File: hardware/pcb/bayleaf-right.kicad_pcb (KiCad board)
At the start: 2 copper layers, 135.5 x 89.5 mm, 64 parts, among them SW1 PG1316S, SW10 PG1316S, SW11 PG1316S, SW12 PG1316S, SW13 PG1316S, SW14 PG1316S, SW15 PG1316S, SW16 PG1316S, SW17 PG1316S, SW18 PG1316S, SW19 PG1316S, SW2 PG1316S, SW20 PG1316S, SW21 PG1316S, SW22 PG1316S, SW23 PG1316S, SW24 PG1316S, SW25 PG1316S, SW26 PG1316S, SW27 PG1316S, SW28 PG1316S, SW29 PG1316S, SW3 PG1316S, SW30 PG1316S, SW31 TS-1187A-B-A-B, SW32 MSK12C02, SW4 PG1316S, SW5 PG1316S, SW6 PG1316S, SW7 PG1316S, SW8 PG1316S, SW9 PG1316S, U1 nice!nano v2

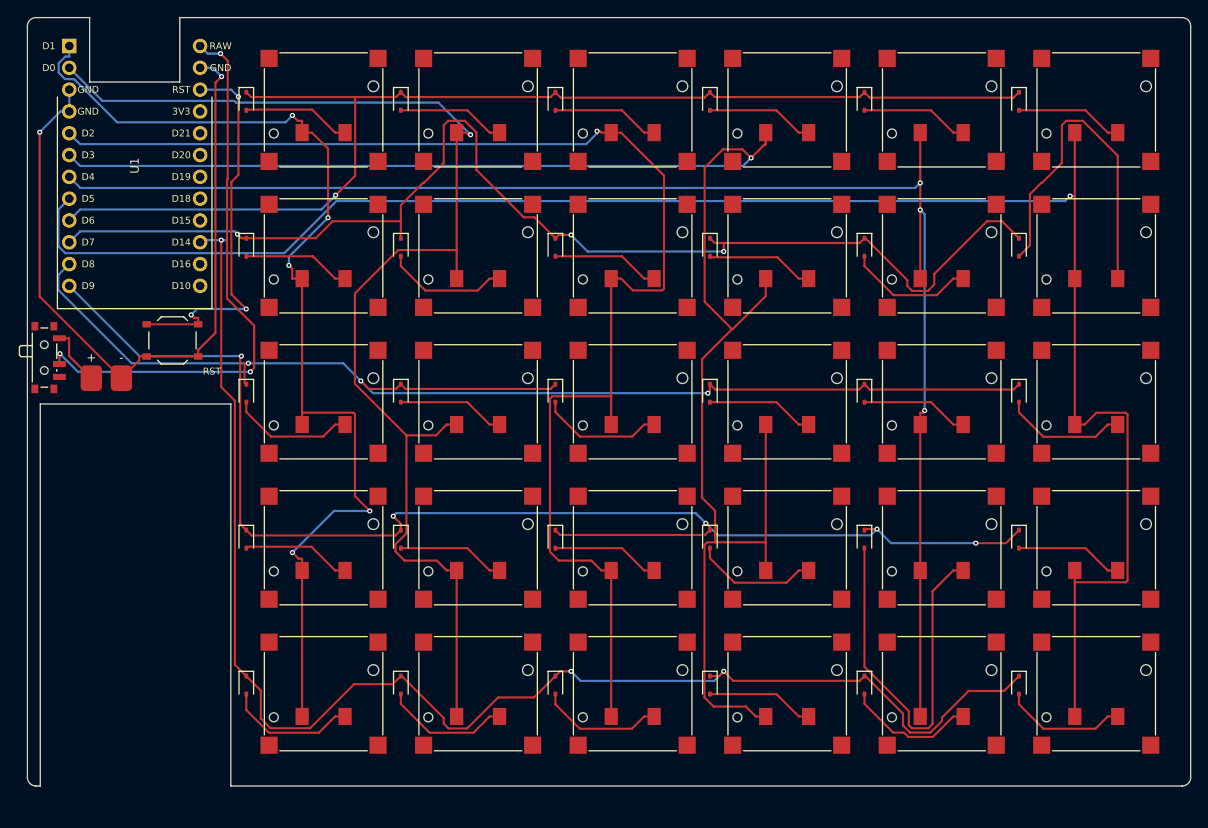
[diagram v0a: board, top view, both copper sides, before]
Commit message: Case: rebuild after the original's MK5 drawing (shell + lid over controller)
- hardware/case: top shell with 103 x 86 key window, 2 mm divider, 27 mm
  controller bay closed by a 0.8 mm roof, 6.2 -> 3.8 mm front curve, drafted
  walls, 7 tapped M2 bosses; separate 0.8 mm bottom plate screwed into them
- PCB: 17 mm pitch to fit the window, SOD-523 diodes, nice!nano rotated so
  USB-C exits the front, 402040 cell under the roof, 2.2 mm holes + copper
  keep-outs at the bosses, per-half matrix pin map; both halves route clean
- firmware: per-half kscan pins in the left/right overlays
- docs: case-drawing notes, BOM/ordering/assembly/schematic, new renders

Co-Authored-By: Claude Opus 5.5 <noreply@anthropic.com>
Claude-Session: https://claude.ai/code/session_01C1HRLCKaYQawWFomwAvAgT
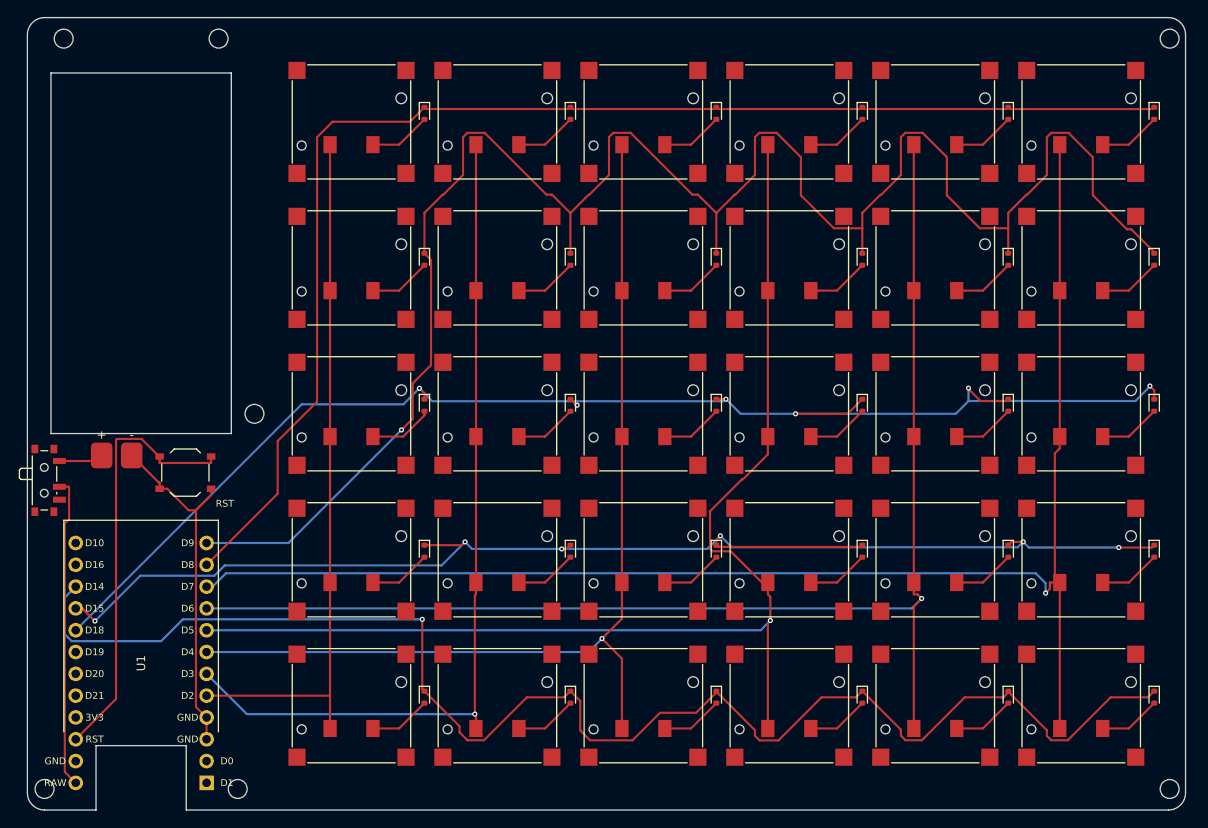
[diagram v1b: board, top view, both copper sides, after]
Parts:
- added H1: boss 6, MountingHole:MountingHole_2.2mm_M2, F.Cu at (133.1, 2.45)
- added H2: boss 6, MountingHole:MountingHole_2.2mm_M2, F.Cu at (133.1, 89.8)
- added H3: boss 6, MountingHole:MountingHole_2.2mm_M2, F.Cu at (22.3, 2.45)
- added H4: boss 6, MountingHole:MountingHole_2.2mm_M2, F.Cu at (4.23, 2.45)
- added H5: boss 6, MountingHole:MountingHole_2.2mm_M2, F.Cu at (26.4, 46.1)
- added H6: boss 4, MountingHole:MountingHole_2.2mm_M2, F.Cu at (24.5, 89.8)
- added H7: boss 4, MountingHole:MountingHole_2.2mm_M2, F.Cu at (2.00, 89.8)
- D1, D10, D11, D12, D13, D14, D15, D16, D17, D18, D19, D2, D20, D21, D22, D23, D24, D25, D26, D27, D28, D29, D3, D30, D4, D5, D6, D7, D8, D9: value 1N4148WS -> 1N4148WT; footprint Diode_SMD:D_SOD-323 -> Diode_SMD:D_SOD-523
- moved U1 58.0 mm to (13.2, 75.2), turned to 180 degrees
- moved D12 20.8 mm to (46.2, 28.1)
- moved D18 20.8 mm to (46.2, 45.1)
- moved D24 20.8 mm to (46.2, 62.1)
- moved D30 20.8 mm to (46.2, 79.2)
- moved D6 20.8 mm to (46.2, 11.2)
- moved D11 19.8 mm to (63.2, 28.1)
- moved D17 19.8 mm to (63.2, 45.1)
- moved D23 19.8 mm to (63.2, 62.1)
- moved D29 19.8 mm to (63.2, 79.2)
- moved D5 19.8 mm to (63.2, 11.2)
- moved D10 18.8 mm to (80.2, 28.1)
- moved D16 18.8 mm to (80.2, 45.1)
- moved D22 18.8 mm to (80.2, 62.1)
- moved D28 18.8 mm to (80.2, 79.2)
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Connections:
- U1 pad 1: COL0 -> (no net)
- U1 pad 10: ROW1 -> COL5
- U1 pad 11: ROW2 -> ROW0
- U1 pad 12: ROW3 -> ROW1
- U1 pad 14: GND -> (no net)
- U1 pad 2: COL1 -> (no net)
- U1 pad 20: (no net) -> ROW2
- U1 pad 21: (no net) -> ROW3
- U1 pad 5: COL2 -> COL0
- U1 pad 6: COL3 -> COL1
- U1 pad 7: COL4 -> COL2
- U1 pad 8: COL5 -> COL3
- U1 pad 9: ROW0 -> COL4
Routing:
- net ROW1: track 142.9 -> 221.8 mm, vias 3 -> 1
- net COL3: track 195.4 -> 142.0 mm
- net COL1: track 147.1 -> 101.3 mm
- net GND: track 86.5 -> 41.0 mm, vias 2 -> 0
- net COL2: track 159.8 -> 116.6 mm
- net COL0: track 124.7 -> 82.4 mm, vias 5 -> 0
- net COL5: track 210.9 -> 170.8 mm
- net N_SW20: track 45.9 -> 7.22 mm
- net N_SW7: track 40.1 -> 7.22 mm
- net RAW: track 66.0 -> 36.4 mm, vias 3 -> 0
- net COL4: track 176.6 -> 152.8 mm, vias 3 -> 1
- net ROW0: track 137.0 -> 154.9 mm, vias 1 -> 0
- net ROW2: track 149.5 -> 160.9 mm, vias 3 -> 6
- net N_SW30: track 15.2 -> 7.22 mm
- net N_SW26: track 15.2 -> 7.22 mm
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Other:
- board size 135.5 x 89.5 mm -> 134.9 x 92.3 mm
- board text added: "LiPo 4.0x20x40"
- board text removed: "LiPo 3.0x20x40"

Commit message: Case: match the build photos - 5 mm tall, separate controller lid
- shell: 3.8 mm frame around the key window curving up to 4.1 mm at the
  controller end; controller bay now open on top; all posts M2 x 2
- new lid part: 0.8 mm plate over the bay, flush with the outer edges, taped
  on; its top is the 5.0 mm tallest point (contrast anodised like the original)
- 302040 cell (bay under the lid is 3.4 mm), 14 x M2x3 screws
- renders: silver shell, blue lid, blank caps; desk/front views like the photos
- docs/BOM/README updated; PCB unchanged

Co-Authored-By: Claude Opus 5.5 <noreply@anthropic.com>
Claude-Session: https://claude.ai/code/session_01C1HRLCKaYQawWFomwAvAgT
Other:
- board text added: "LiPo 3.0x20x40"
- board text removed: "LiPo 4.0x20x40"
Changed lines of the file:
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@@
     (effects (font (size 0.8 0.8) (thickness 0.12)))
   )
-  (gr_text "LiPo 4.0x20x40" (at 13.25 27) (layer "Cmts.User")
+  (gr_text "LiPo 3.0x20x40" (at 13.25 27) (layer "Cmts.User")
     (effects (font (size 0.9 0.9) (thickness 0.135)))
   )

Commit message: Case: one-piece shell from the sketchpad shape (3.2 mm rim, 5.0 mm plateau, S-bends)
- case.py: top surface = blurred square plateau (x >= 96.5, y <= 76) over a 3.2 mm rim;
  controller roofed by the shell (no lid), R2 key-window corners, USB-C in the back wall,
  reset pin-hole, per-post thread depths (2 mm / 1.1 mm)
- PCB: nice!nano USB-C facing the back, KMR2 reset and slide switch beside it, 302030 cell
  window in front of it; rerouted, fab outputs regenerated
- firmware: per-half matrix pins to match the new layout
- docs: sketchpad shape saved, renders, BOM/ordering/assembly/case/schematic updated

Co-Authored-By: Claude Opus 5.5 <noreply@anthropic.com>
Claude-Session: https://claude.ai/code/session_01C1HRLCKaYQawWFomwAvAgT
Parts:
- BT1: footprint bayleaf:Battery_Pads -> bayleaf:Battery_Pads_Small
- H3, H4: value boss 6 -> boss 4
- H6, H7: value boss 4 -> boss 6
- SW31: value TS-1187A-B-A-B -> KMR211NGLFS; footprint Button_Switch_SMD:SW_Push_1P1T_XKB_TS-1187A -> Button_Switch_SMD:SW_Push_1P1T_NO_CK_KMR2
- moved U1 58.2 mm to (13.6, 17.0), turned to 0 degrees
- moved SW32 38.9 mm to (2.10, 15.0)
- moved SW31 31.6 mm to (24.8, 22.0), turned to -90 degrees
- moved BT1 24.2 mm to (2.15, 28.2)
- moved H3 2.48 mm to (24.8, 2.45)
- moved H4 2.23 mm to (2.00, 2.45)
- moved H6 2.23 mm to (22.3, 89.8)
- moved H7 2.23 mm to (4.23, 89.8)
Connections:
- U1 pad 10: COL5 -> ROW2
- U1 pad 11: ROW0 -> ROW1
- U1 pad 12: ROW1 -> ROW0
- U1 pad 17: (no net) -> COL0
- U1 pad 18: (no net) -> COL1
- U1 pad 19: (no net) -> COL2
- U1 pad 20: ROW2 -> COL3
- U1 pad 21: ROW3 -> COL4
- U1 pad 22: ROW4 -> COL5
- U1 pad 5: COL0 -> (no net)
- U1 pad 6: COL1 -> (no net)
- U1 pad 7: COL2 -> (no net)
- U1 pad 8: COL3 -> ROW4
- U1 pad 9: COL4 -> ROW3
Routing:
- net ROW3: track 158.7 -> 199.0 mm
- net ROW4: track 169.9 -> 207.6 mm
- net ROW1: track 221.8 -> 187.9 mm, vias 1 -> 4
- net RST: track 50.5 -> 17.7 mm
- net COL2: track 116.6 -> 129.5 mm, vias 1 -> 3
- net BAT+: track 5.19 -> 15.6 mm
- net ROW0: track 154.9 -> 146.1 mm, vias 0 -> 1
- net COL3: track 142.0 -> 134.3 mm
- net RAW: track 36.4 -> 30.0 mm
- net GND: track 41.0 -> 47.4 mm
- net COL5: track 170.8 -> 176.0 mm
- net COL0: track 82.4 -> 84.6 mm, vias 0 -> 1
- net COL4: track 152.8 -> 150.6 mm
- net ROW2: track 160.9 -> 161.5 mm, vias 6 -> 5
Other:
- outline, holes or cut-outs redrawn
- board text added: "LiPo 3.0x20x30"
- board text removed: "LiPo 3.0x20x40"

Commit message: Drop the power switch, stadium USB-C opening, straight-wall + chamfer case variant
- PCB: no slide switch; the cell feeds the nice!nano RAW pin directly (ZMK deep sleep);
  rerouted, 0 unconnected, courtyard warning gone
- case: obround USB-C opening concentric with the receptacle (continues into the plate
  edge), no switch slot; new bayleaf-shell-*-chamfer variant with vertical walls and a
  1 mm 45 deg chamfer on the top edge that follows the blended surface
- renders: obround receptacle, compare.jpg (drafted vs chamfer); docs and BOM updated

Co-Authored-By: Claude Opus 5.5 <noreply@anthropic.com>
Claude-Session: https://claude.ai/code/session_01C1HRLCKaYQawWFomwAvAgT
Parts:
- removed SW32: MSK12C02, Button_Switch_SMD:SW_SPDT_PCM12
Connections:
- BT1 pad 1: BAT+ -> RAW
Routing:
- net ROW2: track 161.5 -> 178.6 mm, vias 5 -> 6
- net BAT+: track 15.6 -> 0.00 mm
- net ROW1: track 187.9 -> 202.6 mm, vias 4 -> 2
- net COL2: track 129.5 -> 116.7 mm, vias 3 -> 1
- net GND: track 47.4 -> 55.7 mm, vias 0 -> 1
- net COL1: track 100.8 -> 108.1 mm
- net COL5: track 176.0 -> 168.9 mm
- net ROW3: track 199.0 -> 192.9 mm
- net ROW0: track 146.1 -> 140.3 mm
- net ROW4: track 207.6 -> 204.2 mm
- net RAW: track 30.0 -> 32.7 mm
- net COL0: track 84.6 -> 86.6 mm
- net COL3: track 134.3 -> 135.0 mm

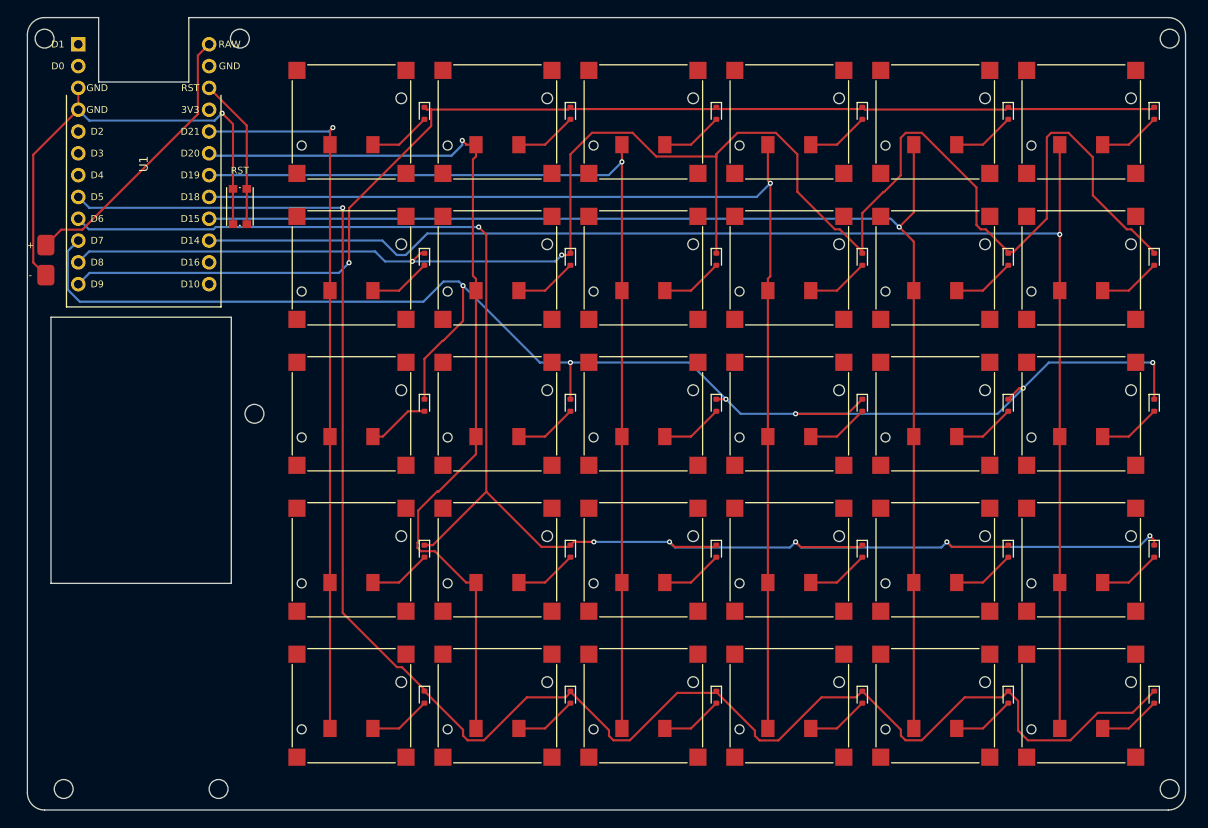
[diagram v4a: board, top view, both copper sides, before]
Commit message: Hand-solderable switches, FR4 bottom plate, reset button on the underside
- PCB: new Kailh_PG1316S_castellated footprint (window under each switch, contacts on plated
  half-holes, soldered from below with an iron; frame anchors on a small hotplate), after
  Mike Holscher's mikecinq, drawn from the Kailh land pattern. Order with castellated holes.
  Routing gets notched keepouts so Freerouting can reach the half-hole pads.
- Reset (KMR2) moves to the bottom side; the pin-hole in the plateau is gone.
- Bottom plate is now a copper-free 0.8 mm FR4 board (generate_pcb.py PlateBuilder, gerbers
  in fab/plate-*) so the radio isn't boxed in by aluminium; windows for the switch solder,
  nice!nano pins, reset button and USB-C.
- Renders (new underside view), BOM, ordering, assembly, case and schematic docs updated.

Co-Authored-By: Claude Opus 5.5 <noreply@anthropic.com>
Claude-Session: https://claude.ai/code/session_01C1HRLCKaYQawWFomwAvAgT
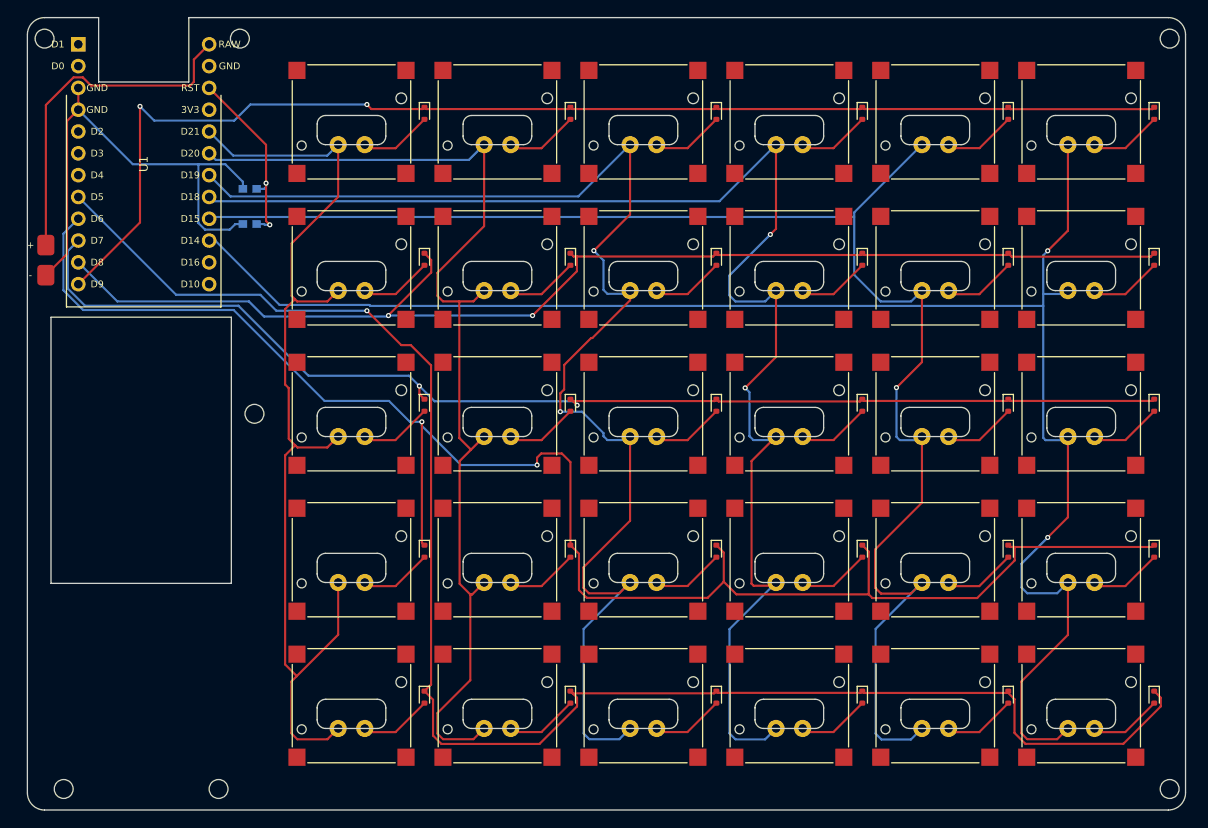
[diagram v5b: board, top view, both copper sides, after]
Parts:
- SW1, SW10, SW11, SW12, SW13, SW14, SW15, SW16, SW17, SW18, SW19, SW2, SW20, SW21, SW22, SW23, SW24, SW25, SW26, SW27, SW28, SW29, SW3, SW30, SW4, SW5, SW6, SW7, SW8, SW9: footprint bayleaf:Kailh_PG1316S -> bayleaf:Kailh_PG1316S_castellated
- SW31: moved to B.Cu
- moved SW31 1.15 mm to (25.9, 22.0), turned to 90 degrees
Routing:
- net ROW1: track 202.6 -> 143.2 mm
- net COL2: track 116.7 -> 154.7 mm, vias 1 -> 2
- net ROW2: track 178.6 -> 142.7 mm, vias 6 -> 2
- net COL0: track 86.6 -> 120.4 mm, vias 1 -> 0
- net COL3: track 135.0 -> 164.6 mm, vias 1 -> 2
- net COL4: track 150.2 -> 177.1 mm
- net COL5: track 168.9 -> 193.9 mm, vias 1 -> 2
- net COL1: track 108.1 -> 123.3 mm, vias 1 -> 0
- net ROW4: track 204.2 -> 192.3 mm
- net RAW: track 32.7 -> 40.6 mm
- net RST: track 17.7 -> 22.1 mm, vias 0 -> 2
- net ROW0: track 140.3 -> 144.4 mm, vias 1 -> 2
- net GND: track 55.7 -> 59.5 mm, vias 1 -> 0
- net N_SW30: track 7.22 -> 8.53 mm
- net N_SW26: track 7.22 -> 8.53 mm
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
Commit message: Switch frame anchors solderable from below: plated holes in the anchor pads
- Kailh_PG1316S_castellated: each 2x2 mm frame-anchor pad gets a 0.7 mm plated hole with a
  1.4 mm pad on the bottom, so the whole switch can be soldered from the underside with an
  iron (hotplate still works). Switch window narrowed to 7.2 mm to keep routing channels.
- Bottom plates: 2.6 mm windows under every anchor hole; silkscreen moved under the battery.
- Router: plain notches again (the 0.3 mm margin choked Freerouting); every attempt is now
  rejected if it leaves copper on a window edge.
- Docs: iron-only switch procedure (untested, try one switch first), hotplate optional.

Co-Authored-By: Claude Opus 5.5 <noreply@anthropic.com>
Claude-Session: https://claude.ai/code/session_01C1HRLCKaYQawWFomwAvAgT
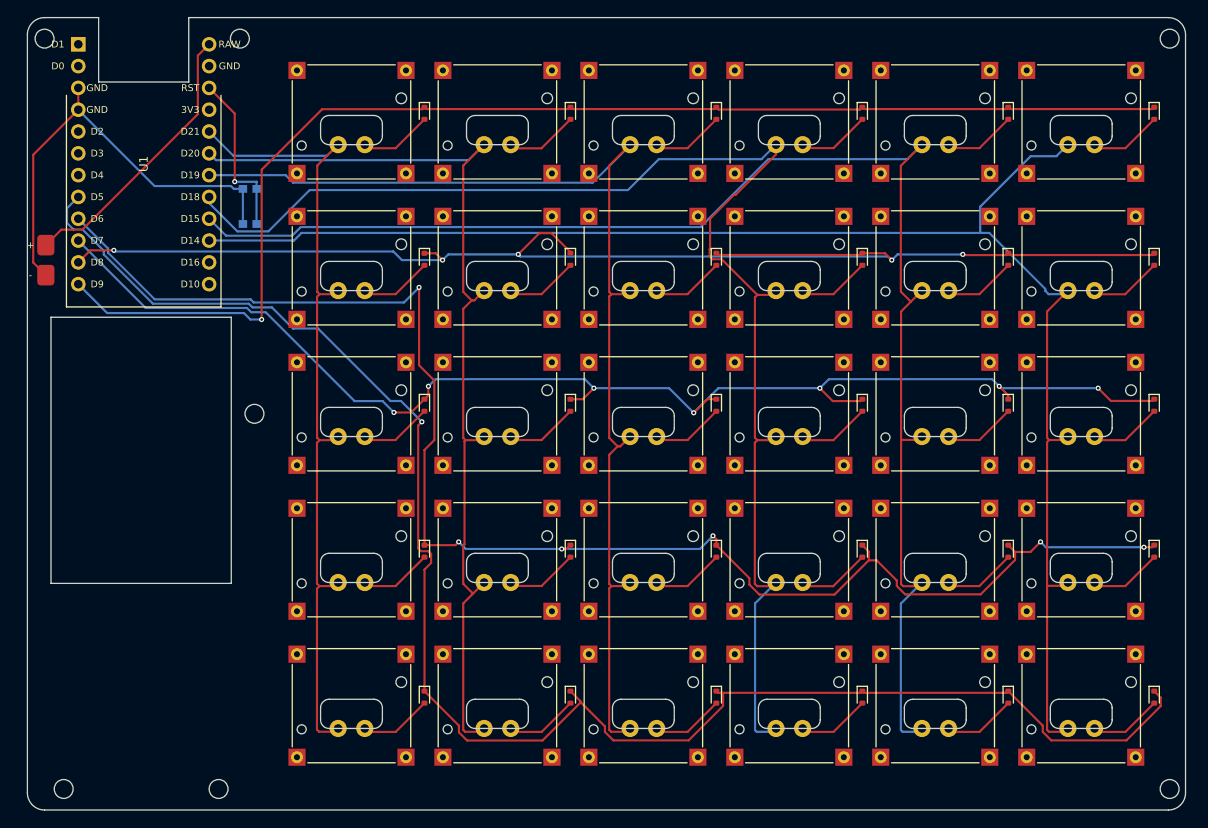
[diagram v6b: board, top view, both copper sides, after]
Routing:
- net COL0: track 120.4 -> 96.4 mm
- net COL2: track 154.7 -> 131.0 mm, vias 2 -> 0
- net ROW1: track 143.2 -> 159.0 mm, vias 2 -> 5
- net ROW3: track 192.0 -> 177.3 mm, vias 2 -> 6
- net COL5: track 193.9 -> 179.9 mm, vias 2 -> 0
- net ROW2: track 142.7 -> 154.4 mm, vias 2 -> 7
- net COL1: track 123.3 -> 113.0 mm
- net RAW: track 40.6 -> 32.7 mm
- net GND: track 59.5 -> 51.7 mm
- net COL4: track 177.1 -> 169.4 mm, vias 1 -> 0
- net COL3: track 164.6 -> 158.4 mm, vias 2 -> 0
- net ROW0: track 144.4 -> 148.4 mm, vias 2 -> 1
- net RST: track 22.1 -> 19.6 mm, vias 2 -> 1
- net ROW4: track 192.3 -> 193.0 mm
